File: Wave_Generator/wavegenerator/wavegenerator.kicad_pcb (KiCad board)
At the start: 2 copper layers, 90.1 x 60 mm, 61 parts, among them J1 01x05, J2 USB_B_Micro, J3 Conn_Coaxial, J4 1x2Pinheader, SW1 button, SW2 button, SW3 SP3T, U1 AZ1117E-3.3, U2 ATmega328P-AU, U3 MC33063AD, U4 MAX038CPP, Y1 16MHz

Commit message: naming changes
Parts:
- C1, C2: value 100uF -> 220uF 10V
- J1: footprint wavegenerator_v1:01x05_pin_header -> wavegenerator:01x05_pin_header
- J2: footprint wavegenerator_v1:USB_Micro-B_Amphenol_10118194-0001LF_Horizontal -> wavegenerator:USB_Micro-B_Amphenol_10118194-0001LF_Horizontal
- J3: footprint wavegenerator_v1:BNC_connector_731000105 -> wavegenerator:BNC_connector_731000105
- MOD1: footprint wavegenerator_v1:TFT_LCD_ST7735 -> wavegenerator:TFT_LCD_ST7735
- R1, R2: value 51 -> 182k
- R101: value 0.24 -> 1.5
- R102: value 3.32k -> 3.32k 1%
- R103: value 10k -> 10k 1%
- R5: value 180k -> 182k 1%
- R6: value 560 -> 549 1%
- R7, R8, R9: value 560 -> 549
- RV1, RV2, RV3: footprint wavegenerator_v1:Potentiometer_PTV09A -> wavegenerator:Potentiometer_PTV09A
- SW3: footprint wavegenerator_v1:SP3T_OS103011MS8QP1 -> wavegenerator:SP3T_OS103011MS8QP1
- TP7: value output -> MAX038 Out
- U4: footprint wavegenerator_v1:MAX038CPP-W -> wavegenerator:MAX038CPP-W
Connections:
- C3 pad 2: /output -> /MAX038_output
- J3 pad 1: Net-(J3-Pad1) -> /output
- J4 pad 1: Net-(J3-Pad1) -> /output
- R8 pad 1: /output -> /MAX038_output
- R9 pad 1: Net-(J3-Pad1) -> /output
- RV3 pad 3: /output -> /MAX038_output
- TP7 pad 1: /output -> /MAX038_output
- U4 pad 13: GND -> Net-(U4-Pad13)
- U4 pad 18: GND -> Net-(U4-Pad18)
- U4 pad 19: /output -> /MAX038_output
- U4 pad 2: GND -> Net-(U4-Pad2)
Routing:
- net /MAX038_output: track 0.00 -> 63.0 mm, vias 0 -> 1
- net /output: track 63.0 -> 29.8 mm, vias 1 -> 0
- net Net-(J3-Pad1): track 29.8 -> 0.00 mm

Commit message: some layout changes
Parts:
- removed the C5 at (81.0, 70.4)
- removed the C7 at (81.0, 79.5)
- moved C5 4.55 mm to (83.5, 70.3)
- renumbered C6 to C5, C8 to C6, C9 to C7, C10 to C8, C11 to C9, D1 to D101, L1 to L101, U2 to U1, U1 to U101, U3 to U102, U4 to U2, Y1 to Y101
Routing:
- net -5V: track 56.0 -> 59.2 mm
- net +5V: vias 1 -> 2

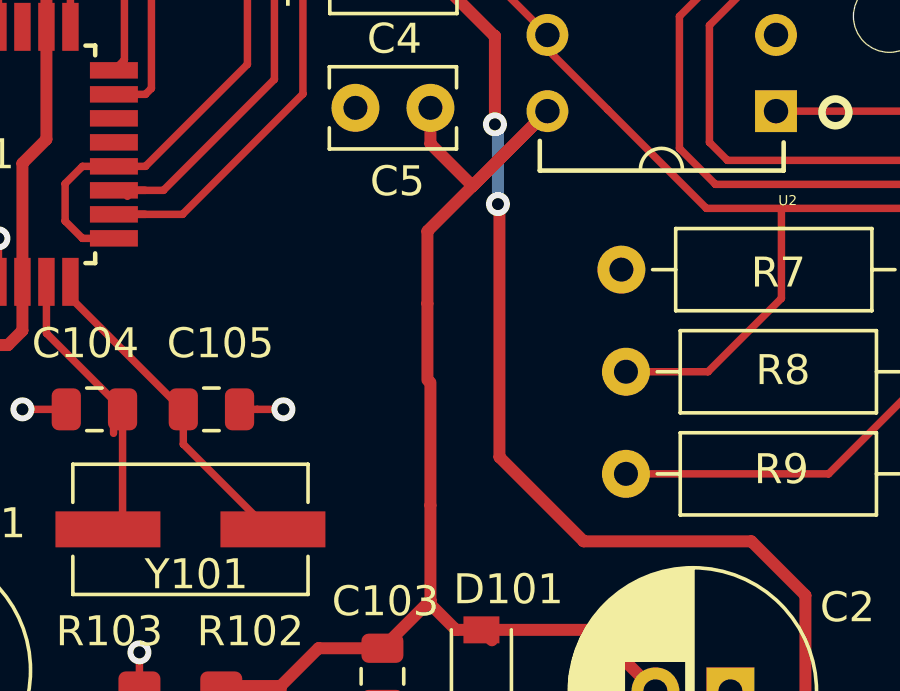
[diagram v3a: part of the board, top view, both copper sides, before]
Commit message: oscilloscope instructions
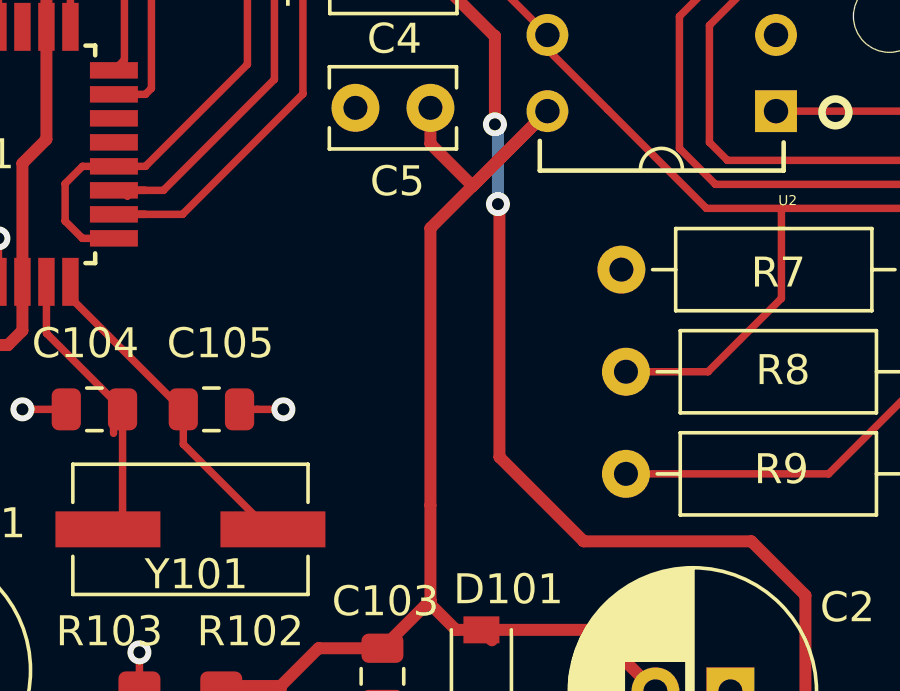
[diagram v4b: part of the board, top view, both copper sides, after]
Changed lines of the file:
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@@
     (thickness 1.6)
     (drawings 32)
-    (tracks 432)
+    (tracks 430)
     (zones 0)
     (modules 59)
@@
   (segment (start 78.50875 89.6225) (end 79.76875 88.3625) (width 0.4) (layer F.Cu) (net 2))
   (segment (start 76.5284 89.6225) (end 78.50875 89.6225) (width 0.4) (layer F.Cu) (net 2))
-  (segment (start 83.5 79.5) (end 83.5 83.6) (width 0.4) (layer F.Cu) (net 2))
   (segment (start 83.5 86.7625) (end 81.9 88.3625) (width 0.4) (layer F.Cu) (net 2))
-  (segment (start 83.5 83.6) (end 83.5 86.7625) (width 0.4) (layer F.Cu) (net 2))
   (segment (start 83.5 86.9) (end 83.5 86.7625) (width 0.4) (layer F.Cu) (net 2))
   (segment (start 84.35 87.75) (end 83.5 86.9) (width 0.4) (layer F.Cu) (net 2))
@@
   (segment (start 83.5 70.35) (end 83.5 71.55) (width 0.4) (layer F.Cu) (net 2))
   (segment (start 87.4 70.46) (end 84.905 72.955) (width 0.4) (layer F.Cu) (net 2))
-  (segment (start 83.4 76.875) (end 83.4 79.4248) (width 0.4) (layer F.Cu) (net 2))
-  (segment (start 83.4 74.46) (end 83.4 76.875) (width 0.4) (layer F.Cu) (net 2))
-  (segment (start 84.905 72.955) (end 83.4 74.46) (width 0.4) (layer F.Cu) (net 2))
+  (segment (start 83.5 83.6) (end 83.5 86.7625) (width 0.4) (layer F.Cu) (net 2))
+  (segment (start 83.5 74.36) (end 83.5 83.6) (width 0.4) (layer F.Cu) (net 2))
+  (segment (start 84.905 72.955) (end 83.5 74.36) (width 0.4) (layer F.Cu) (net 2))
   (segment (start 53.8804 96.9772) (end 54.101 96.9772) (width 0.4) (layer F.Cu) (net 3))
   (segment (start 50.0844 93.1812) (end 53.8804 96.9772) (width 0.4) (layer F.Cu) (net 3))

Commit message: small changes
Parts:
- renumbered J2 to J101, U2 to U1, U1 to U103

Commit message: Logos
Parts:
- added G***: LOGO, wavegenerator:Logog_4, B.Cu at (90.1, 63.2)
